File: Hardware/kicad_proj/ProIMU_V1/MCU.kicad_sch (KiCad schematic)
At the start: 8 parts, among them U10 STM32F412RETx

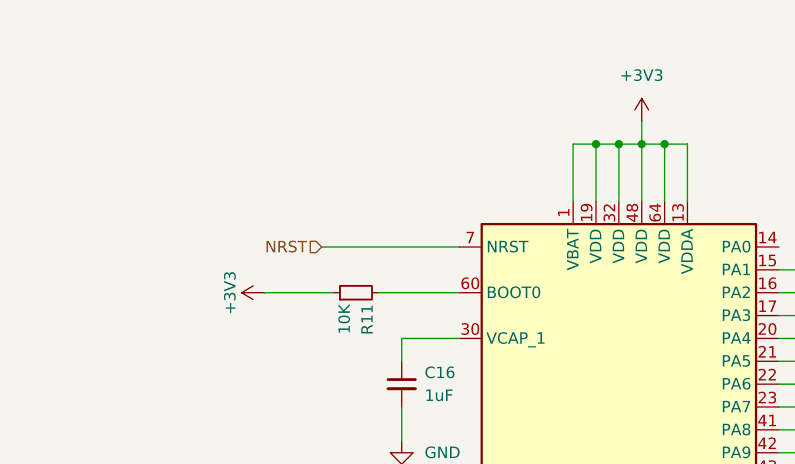
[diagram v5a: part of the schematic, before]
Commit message: Updated schematic and layout
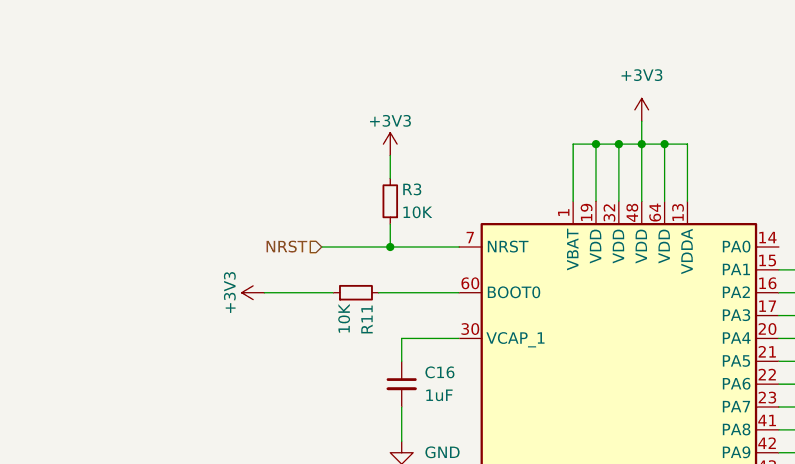
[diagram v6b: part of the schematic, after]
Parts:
- added R3: 10K, Resistor_SMD:R_0402_1005Metric_Pad0.72x0.64mm_HandSolder, symbol Device:R_Small
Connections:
- net +3V3: now also R3.2
- net NRST: now also R3.1
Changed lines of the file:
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@@
   (junction (at 240.03 50.8) (diameter 0) (color 0 0 0 0)
+  )
+  (junction (at 132.08 57.15) (diameter 0) (color 0 0 0 0)
   )
   (junction (at 259.08 38.1) (diameter 0) (color 0 0 0 0)
@@
     (stroke (width 0) (type default) (color 0 0 0 0))
   )
+  (wire (pts (xy 132.08 54.61) (xy 132.08 57.15))
+    (stroke (width 0) (type default) (color 0 0 0 0))
+  )
   (wire (pts (xy 114.3 100.33) (xy 139.7 100.33))
     (stroke (width 0) (type default) (color 0 0 0 0))
@@
     (stroke (width 0) (type default) (color 0 0 0 0))
   )
-  (wire (pts (xy 124.46 57.15) (xy 139.7 57.15))
+  (wire (pts (xy 124.46 57.15) (xy 132.08 57.15))
     (stroke (width 0) (type default) (color 0 0 0 0))
   )
@@
     (stroke (width 0) (type default) (color 0 0 0 0))
   )
+  (wire (pts (xy 132.08 46.99) (xy 132.08 49.53))
+    (stroke (width 0) (type default) (color 0 0 0 0))
+  )
   (wire (pts (xy 114.3 97.79) (xy 139.7 97.79))
     (stroke (width 0) (type default) (color 0 0 0 0))
@@
   )
   (wire (pts (xy 157.48 45.72) (xy 160.02 45.72))
+    (stroke (width 0) (type default) (color 0 0 0 0))
+  )
+  (wire (pts (xy 132.08 57.15) (xy 139.7 57.15))
     (stroke (width 0) (type default) (color 0 0 0 0))
   )
@@
     (pin "9")
   )
+  (symbol (lib_id "power:+3V3") (at 132.08 46.99 0) (mirror y) (unit 1)
+    (in_bom yes) (on_board yes)
+    (property "Reference" "#PWR08" (id 0) (at 132.08 50.8 0)
+      (effects (font (size 1.27 1.27)) hide)
+    )
+    (property "Value" "+3V3" (id 1) (at 132.08 43.18 0))
+    (property "Footprint" "" (id 2) (at 132.08 46.99 0)
+      (effects (font (size 1.27 1.27)) hide)
+    )
+    (property "Datasheet" "" (id 3) (at 132.08 46.99 0)
+      (effects (font (size 1.27 1.27)) hide)
+    )
+    (pin "1")
+  )
   (symbol (lib_id "Device:C_Small") (at 267.97 44.45 0) (unit 1)
     (in_bom yes) (on_board yes) (fields_autoplaced)
@@
       (effects (font (size 1.27 1.27)) hide)
     )
+    (pin "1")
+    (pin "2")
+  )
+  (symbol (lib_id "Device:R_Small") (at 132.08 52.07 180) (unit 1)
+    (in_bom yes) (on_board yes)
+    (property "Reference" "R3" (id 0) (at 133.35 50.8 0)
+      (effects (font (size 1.27 1.27)) (justify right))
+    )
+    (property "Value" "10K" (id 1) (at 133.35 53.34 0)
+      (effects (font (size 1.27 1.27)) (justify right))
+    )
+    (property "Footprint" "Resistor_SMD:R_0402_1005Metric_Pad0.72x0.64mm_HandSolder" (id 2) (at 132.08 52.07 0)
+      (effects (font (size 1.27 1.27)) hide)
+    )
+    (property "Datasheet" "~" (id 3) (at 132.08 52.07 0)
+      (effects (font (size 1.27 1.27)) hide)
+    )

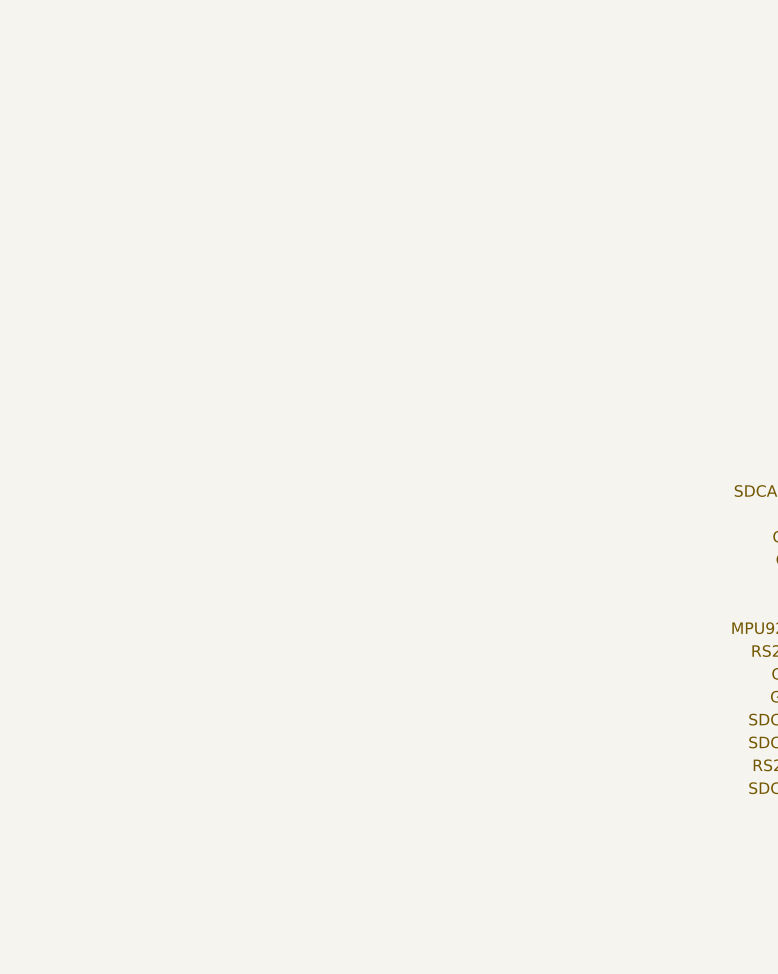
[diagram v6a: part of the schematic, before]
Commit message: Added sensor schematic
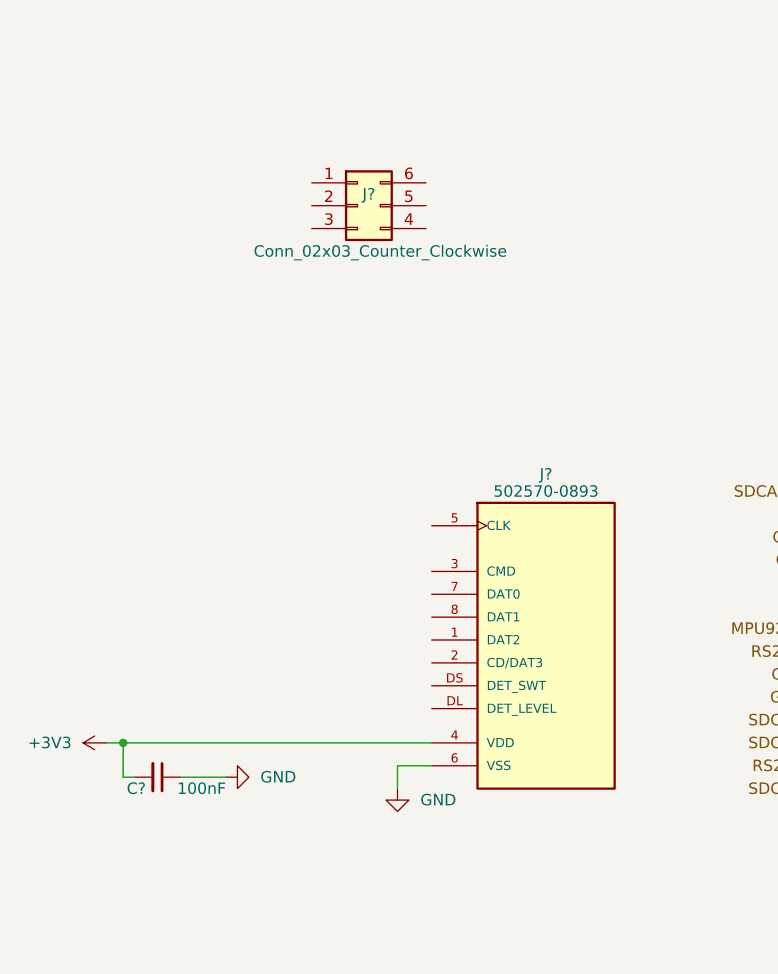
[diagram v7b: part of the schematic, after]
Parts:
- added C?: 100nF, Capacitor_SMD:C_0402_1005Metric_Pad0.74x0.62mm_HandSolder, symbol Device:C_Small
- added J?: 502570-0893, footprints:MOLEX_502570-0893, symbol 502570-0893:502570-0893
- added J?: Conn_02x03_Counter_Clockwise, Connector_PinHeader_2.54mm:PinHeader_2x03_P2.54mm_Vertical_SMD, symbol Connector_Generic:Conn_02x03_Counter_Clockwise
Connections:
- net +3V3: now also C?.2, J?.4 (VDD)
- net GND: now also C?.1, J?.6 (VSS)
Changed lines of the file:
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@@
   (junction (at 240.03 50.8) (diameter 0) (color 0 0 0 0)
   )
+  (junction (at 27.305 120.65) (diameter 0) (color 0 0 0 0)
+  )
   (junction (at 132.08 57.15) (diameter 0) (color 0 0 0 0)
   )
@@
   )
   (no_connect (at 139.7 105.41))
+  (wire (pts (xy 57.785 123.19) (xy 57.785 125.73))
+    (stroke (width 0) (type default) (color 0 0 0 0))
+  )
   (wire (pts (xy 229.87 38.1) (xy 240.03 38.1))
     (stroke (width 0) (type default) (color 0 0 0 0))
@@
     (stroke (width 0) (type default) (color 0 0 0 0))
   )
+  (wire (pts (xy 25.4 120.65) (xy 27.305 120.65))
+    (stroke (width 0) (type default) (color 0 0 0 0))
+  )
   (wire (pts (xy 160.02 43.18) (xy 160.02 45.72))
     (stroke (width 0) (type default) (color 0 0 0 0))
@@
     (stroke (width 0) (type default) (color 0 0 0 0))
   )
+  (wire (pts (xy 27.305 120.65) (xy 61.595 120.65))
+    (stroke (width 0) (type default) (color 0 0 0 0))
+  )
+  (wire (pts (xy 28.575 124.46) (xy 27.305 124.46))
+    (stroke (width 0) (type default) (color 0 0 0 0))
+  )
   (wire (pts (xy 139.7 113.03) (xy 114.3 113.03))
     (stroke (width 0) (type default) (color 0 0 0 0))
@@
     (stroke (width 0) (type default) (color 0 0 0 0))
   )
+  (wire (pts (xy 61.595 123.19) (xy 57.785 123.19))
+    (stroke (width 0) (type default) (color 0 0 0 0))
+  )
   (wire (pts (xy 165.1 52.07) (xy 165.1 45.72))
     (stroke (width 0) (type default) (color 0 0 0 0))
@@
     (stroke (width 0) (type default) (color 0 0 0 0))
   )
+  (wire (pts (xy 27.305 120.65) (xy 27.305 124.46))
+    (stroke (width 0) (type default) (color 0 0 0 0))
+  )
   (wire (pts (xy 175.26 135.89) (xy 200.66 135.89))
     (stroke (width 0) (type default) (color 0 0 0 0))
@@
     (stroke (width 0) (type default) (color 0 0 0 0))
   )
+  (wire (pts (xy 33.655 124.46) (xy 38.735 124.46))
+    (stroke (width 0) (type default) (color 0 0 0 0))
+  )
   (wire (pts (xy 229.87 50.8) (xy 240.03 50.8))
     (stroke (width 0) (type default) (color 0 0 0 0))
@@
   (hierarchical_label "SDCARD_SDIO_CMD" (shape input) (at 114.3 92.71 180)
     (effects (font (size 1.27 1.27)) (justify right))
+  )
+  (symbol (lib_id "power:GND") (at 38.735 124.46 90) (unit 1)
+    (in_bom yes) (on_board yes) (fields_autoplaced)
+    (property "Reference" "#PWR?" (id 0) (at 45.085 124.46 0)
+      (effects (font (size 1.27 1.27)) hide)
+    )
+    (property "Value" "GND" (id 1) (at 42.545 124.4599 90)
+      (effects (font (size 1.27 1.27)) (justify right))
+    )
+    (property "Footprint" "" (id 2) (at 38.735 124.46 0)
+      (effects (font (size 1.27 1.27)) hide)
+    )
+    (property "Datasheet" "" (id 3) (at 38.735 124.46 0)
+      (effects (font (size 1.27 1.27)) hide)
+    )
+    (pin "1")
   )
   (symbol (lib_id "power:+3V3") (at 118.11 62.23 90) (mirror x) (unit 1)
@@
     (pin "9")
   )
+  (symbol (lib_id "Device:C_Small") (at 31.115 124.46 270) (mirror x) (unit 1)
+    (in_bom yes) (on_board yes)
+    (property "Reference" "C?" (id 0) (at 29.845 125.73 90)
+      (effects (font (size 1.27 1.27)) (justify right))
+    )
+    (property "Value" "100nF" (id 1) (at 38.735 125.73 90)
+      (effects (font (size 1.27 1.27)) (justify right))
+    )
+    (property "Footprint" "Capacitor_SMD:C_0402_1005Metric_Pad0.74x0.62mm_HandSolder" (id 2) (at 31.115 124.46 0)
+      (effects (font (size 1.27 1.27)) hide)
+    )
+    (property "Datasheet" "~" (id 3) (at 31.115 124.46 0)
+      (effects (font (size 1.27 1.27)) hide)
+    )
+    (pin "1")
+    (pin "2")
+  )
   (symbol (lib_id "power:+3V3") (at 132.08 46.99 0) (mirror y) (unit 1)
     (in_bom yes) (on_board yes)
@@
     (pin "2")
   )
+  (symbol (lib_id "power:GND") (at 57.785 125.73 0) (unit 1)
+    (in_bom yes) (on_board yes) (fields_autoplaced)
+    (property "Reference" "#PWR?" (id 0) (at 57.785 132.08 0)
+      (effects (font (size 1.27 1.27)) hide)
+    )
+    (property "Value" "GND" (id 1) (at 60.325 126.9999 0)
+      (effects (font (size 1.27 1.27)) (justify left))
+    )
+    (property "Footprint" "" (id 2) (at 57.785 125.73 0)
+      (effects (font (size 1.27 1.27)) hide)
+    )
+    (property "Datasheet" "" (id 3) (at 57.785 125.73 0)
+      (effects (font (size 1.27 1.27)) hide)
+    )
+    (pin "1")
+  )
+  (symbol (lib_id "power:+3V3") (at 25.4 120.65 90) (unit 1)
+    (in_bom yes) (on_board yes) (fields_autoplaced)
+    (property "Reference" "#PWR?" (id 0) (at 29.21 120.65 0)
+      (effects (font (size 1.27 1.27)) hide)
+    )
+    (property "Value" "+3V3" (id 1) (at 21.59 120.6499 90)
+      (effects (font (size 1.27 1.27)) (justify left))
+    )
+    (property "Footprint" "" (id 2) (at 25.4 120.65 0)
+      (effects (font (size 1.27 1.27)) hide)
+    )
+    (property "Datasheet" "" (id 3) (at 25.4 120.65 0)
+      (effects (font (size 1.27 1.27)) hide)
+    )
+    (pin "1")
+  )
   (symbol (lib_id "Device:C_Small") (at 240.03 44.45 0) (unit 1)
     (in_bom yes) (on_board yes) (fields_autoplaced)
@@
     (pin "2")
   )
+  (symbol (lib_id "502570-0893:502570-0893") (at 79.375 106.68 0) (unit 1)
+    (in_bom yes) (on_board yes)
+    (property "Reference" "J?" (id 0) (at 74.295 90.805 0))
+    (property "Value" "502570-0893" (id 1) (at 74.295 92.71 0))
+    (property "Footprint" "footprints:MOLEX_502570-0893" (id 2) (at 79.375 106.68 0)
+      (effects (font (size 1.27 1.27)) (justify left bottom) hide)
+    )
+    (property "Datasheet" "" (id 3) (at 79.375 106.68 0)
+      (effects (font (size 1.27 1.27)) (justify left bottom) hide)
+    )
+    (pin "1")
+    (pin "2")
+    (pin "3")
+    (pin "4")
+    (pin "5")
+    (pin "6")
+    (pin "7")
+    (pin "8")
+    (pin "DL")
+    (pin "DS")
+  )
+  (symbol (lib_id "Connector_Generic:Conn_02x03_Counter_Clockwise") (at 53.34 60.96 0) (unit 1)
+    (in_bom yes) (on_board yes)
+    (property "Reference" "J?" (id 0) (at 54.61 59.69 0))
+    (property "Value" "Conn_02x03_Counter_Clockwise" (id 1) (at 55.88 66.04 0))
+    (property "Footprint" "Connector_PinHeader_2.54mm:PinHeader_2x03_P2.54mm_Vertical_SMD" (id 2) (at 53.34 60.96 0)
+      (effects (font (size 1.27 1.27)) hide)
+    )
+    (property "Datasheet" "~" (id 3) (at 53.34 60.96 0)
+      (effects (font (size 1.27 1.27)) hide)
+    )
+    (pin "1")
+    (pin "2")
+    (pin "3")
+    (pin "4")
+    (pin "5")
+    (pin "6")
+  )
 )

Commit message: Updated Schematic and Layout
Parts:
- gave numbers to parts that had none: 3
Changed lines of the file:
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@@
   (symbol (lib_id "power:GND") (at 38.735 124.46 90) (unit 1)
     (in_bom yes) (on_board yes) (fields_autoplaced)
-    (property "Reference" "#PWR?" (id 0) (at 45.085 124.46 0)
+    (property "Reference" "#PWR0106" (id 0) (at 45.085 124.46 0)
       (effects (font (size 1.27 1.27)) hide)
     )
@@
   (symbol (lib_id "Device:C_Small") (at 31.115 124.46 270) (mirror x) (unit 1)
     (in_bom yes) (on_board yes)
-    (property "Reference" "C?" (id 0) (at 29.845 125.73 90)
+    (property "Reference" "C3" (id 0) (at 29.845 125.73 90)
       (effects (font (size 1.27 1.27)) (justify right))
     )
@@
   (symbol (lib_id "power:GND") (at 57.785 125.73 0) (unit 1)
     (in_bom yes) (on_board yes) (fields_autoplaced)
-    (property "Reference" "#PWR?" (id 0) (at 57.785 132.08 0)
+    (property "Reference" "#PWR0107" (id 0) (at 57.785 132.08 0)
       (effects (font (size 1.27 1.27)) hide)
     )
@@
   (symbol (lib_id "power:+3V3") (at 25.4 120.65 90) (unit 1)
     (in_bom yes) (on_board yes) (fields_autoplaced)
-    (property "Reference" "#PWR?" (id 0) (at 29.21 120.65 0)
+    (property "Reference" "#PWR0108" (id 0) (at 29.21 120.65 0)
       (effects (font (size 1.27 1.27)) hide)
     )
@@
   (symbol (lib_id "502570-0893:502570-0893") (at 79.375 106.68 0) (unit 1)
     (in_bom yes) (on_board yes)
-    (property "Reference" "J?" (id 0) (at 74.295 90.805 0))
+    (property "Reference" "J2" (id 0) (at 74.295 90.805 0))
     (property "Value" "502570-0893" (id 1) (at 74.295 92.71 0))
     (property "Footprint" "footprints:MOLEX_502570-0893" (id 2) (at 79.375 106.68 0)
@@
   (symbol (lib_id "Connector_Generic:Conn_02x03_Counter_Clockwise") (at 53.34 60.96 0) (unit 1)
     (in_bom yes) (on_board yes)
-    (property "Reference" "J?" (id 0) (at 54.61 59.69 0))
+    (property "Reference" "J1" (id 0) (at 54.61 59.69 0))
     (property "Value" "Conn_02x03_Counter_Clockwise" (id 1) (at 55.88 66.04 0))
     (property "Footprint" "Connector_PinHeader_2.54mm:PinHeader_2x03_P2.54mm_Vertical_SMD" (id 2) (at 53.34 60.96 0)
